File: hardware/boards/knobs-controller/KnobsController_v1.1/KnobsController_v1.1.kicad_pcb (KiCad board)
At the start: 2 copper layers, 110.5 x 54.3 mm, 71 parts, among them J1 ZX62-AB-5PA(31), J4 JST---S4B-PH-SM4-TB(LF)(SN)_J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, U2 MK1_ZERO_AP7215-33YG-13, U3 MK1_ZERO_ATSAMD21G18A-48, Y1 32.768KHz

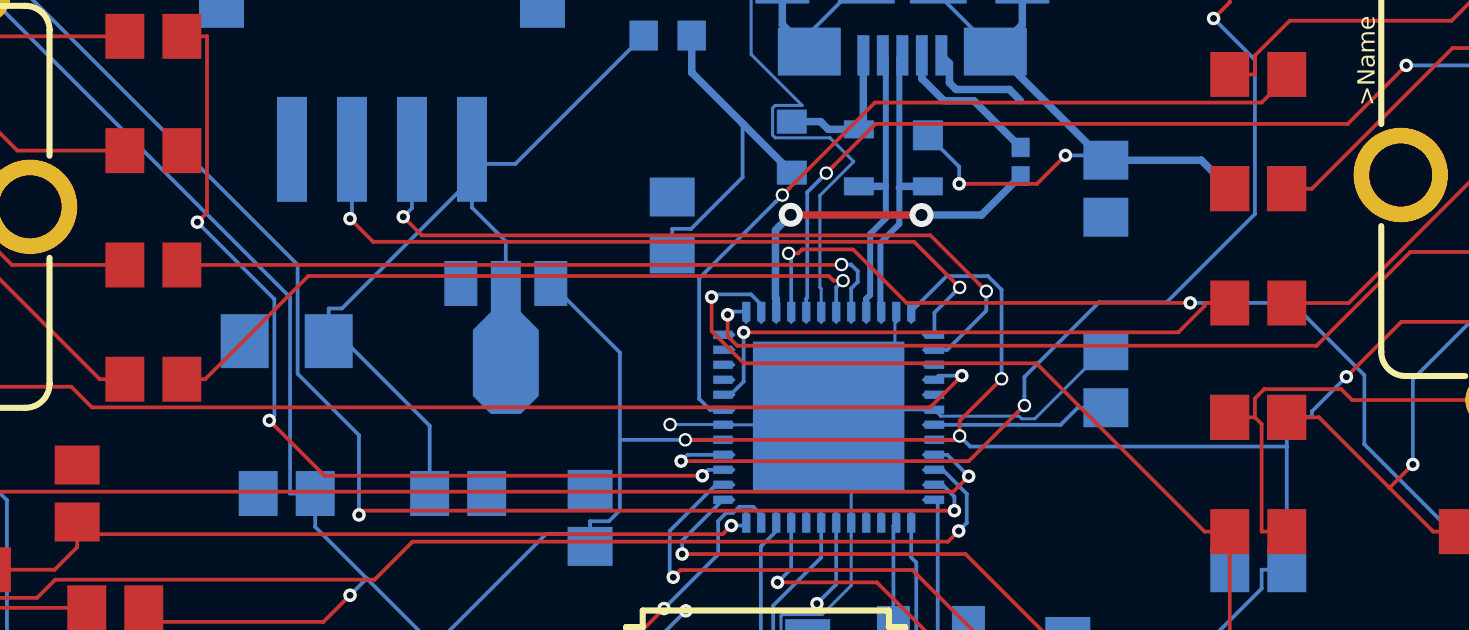
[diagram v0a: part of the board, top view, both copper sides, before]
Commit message: fixed unconnected traces
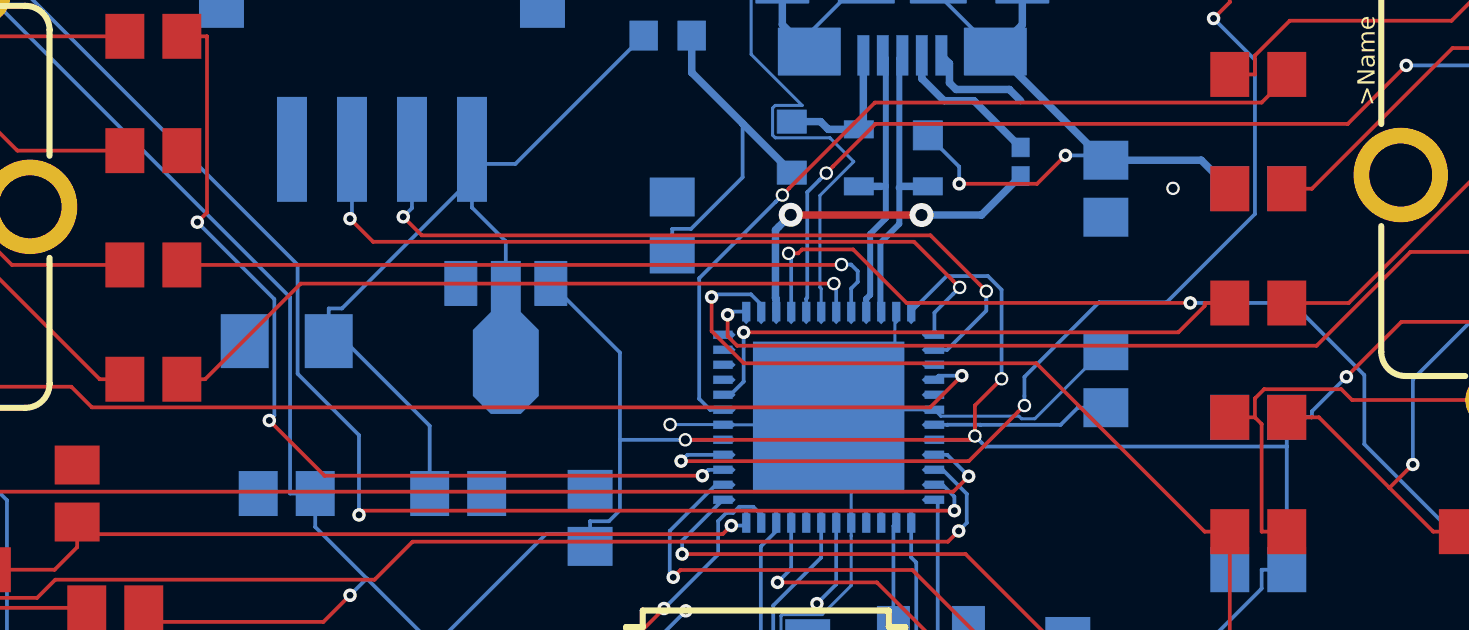
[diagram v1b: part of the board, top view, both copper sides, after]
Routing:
- net PA22_TC4-W0: track 24.7 -> 24.0 mm
- net GND: vias 1 -> 2
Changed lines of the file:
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@@
     (thickness 1.6)
     (drawings 240)
-    (tracks 659)
+    (tracks 663)
     (zones 0)
     (modules 71)
@@
     (31 Bottom signal)
     (32 B.Adhes user)
-    (33 F.Adhes user hide)
+    (33 F.Adhes user)
     (34 B.Paste user)
     (35 F.Paste user)
@@
   )
   (setup
-    (last_trace_width 0.1016)
+    (last_trace_width 0.0889)
     (user_trace_width 0.1016)
     (user_trace_width 0.2032)
@@
     (effects (font (size 1.6891 1.6891) (thickness 0.14224)) (justify left bottom))
   )
-  (via (at 154.432 112.776) (size 0.45) (drill 0.3) (layers Top Bottom) (net 25))
   (segment (start 153.821 100.087) (end 154.092 100.358) (width 0.25) (layer Bottom) (net 1))
   (segment (start 154.092 100.358) (end 154.092 101.006) (width 0.25) (layer Bottom) (net 1))
@@
   (segment (start 153.80171 112.11471) (end 156.405952 112.11471) (width 0.1016) (layer Bottom) (net 1))
   (segment (start 153.591 111.904) (end 153.80171 112.11471) (width 0.1016) (layer Bottom) (net 1))
+  (via (at 161.544 104.521) (size 0.45) (drill 0.3) (layers Top Bottom) (net 1))
   (segment (start 154.2562 115.2656) (end 154.2562 114.7965) (width 0.125) (layer Bottom) (net 4))
   (segment (start 154.2562 114.7965) (end 153.8637 114.404) (width 0.125) (layer Bottom) (net 4))
@@
   (segment (start 124.2638 117.234) (end 125.016 116.4818) (width 0.125) (layer Top) (net 9))
   (via (at 146.8211 115.7612) (size 0.45) (layers Top Bottom) (net 9))
-  (segment (start 129.281 110.884) (end 132.722946 107.442054) (width 0.125) (layer Top) (net 10))
-  (segment (start 150.070956 107.442054) (end 150.226506 107.597604) (width 0.125) (layer Top) (net 10))
+  (segment (start 150.316 108.629) (end 150.316 107.771) (width 0.125) (layer Bottom) (net 10))
+  (via (at 150.241 107.696) (size 0.45) (drill 0.3) (layers Top Bottom) (net 10))
   (segment (start 128.506 110.884) (end 129.281 110.884) (width 0.125) (layer Top) (net 10))
-  (segment (start 150.226506 107.597604) (end 150.544704 107.597604) (width 0.125) (layer Top) (net 10))
-  (segment (start 132.722946 107.442054) (end 150.070956 107.442054) (width 0.125) (layer Top) (net 10))
-  (segment (start 150.316 107.826308) (end 150.319705 107.822603) (width 0.125) (layer Bottom) (net 10))
-  (via (at 150.544704 107.597604) (size 0.45) (drill 0.3) (layers Top Bottom) (net 10))
-  (segment (start 150.319705 107.822603) (end 150.544704 107.597604) (width 0.125) (layer Bottom) (net 10))
-  (segment (start 150.316 108.629) (end 150.316 107.826308) (width 0.125) (layer Bottom) (net 10))
-  (via (at 150.495 107.061) (size 0.45) (drill 0.3) (layers Top Bottom) (net 11))
-  (segment (start 150.482 107.074) (end 150.495 107.061) (width 0.125) (layer Top) (net 11))
-  (segment (start 151.034531 107.282333) (end 150.813198 107.061) (width 0.125) (layer Bottom) (net 11))
-  (segment (start 128.506 107.074) (end 150.482 107.074) (width 0.125) (layer Top) (net 11))
-  (segment (start 150.816 107.858532) (end 151.034531 107.640001) (width 0.125) (layer Bottom) (net 11))
-  (segment (start 150.813198 107.061) (end 150.495 107.061) (width 0.125) (layer Bottom) (net 11))
+  (segment (start 150.316 107.771) (end 150.241 107.696) (width 0.125) (layer Bottom) (net 10))
+  (segment (start 129.281 110.884) (end 132.469 107.696) (width 0.125) (layer Top) (net 10))
+  (segment (start 132.469 107.696) (end 150.241 107.696) (width 0.125) (layer Top) (net 10))
+  (segment (start 150.813196 107.060976) (end 150.494998 107.060976) (width 0.125) (layer Bottom) (net 11))
+  (segment (start 151.034531 107.640001) (end 151.034531 107.282311) (width 0.125) (layer Bottom) (net 11))
+  (segment (start 150.481974 107.074) (end 150.494998 107.060976) (width 0.125) (layer Top) (net 11))
+  (segment (start 128.506 107.074) (end 150.481974 107.074) (width 0.125) (layer Top) (net 11))
   (segment (start 150.816 108.629) (end 150.816 107.858532) (width 0.125) (layer Bottom) (net 11))
-  (segment (start 151.034531 107.640001) (end 151.034531 107.282333) (width 0.125) (layer Bottom) (net 11))
+  (segment (start 151.034531 107.282311) (end 150.813196 107.060976) (width 0.125) (layer Bottom) (net 11))
+  (segment (start 150.816 107.858532) (end 151.034531 107.640001) (width 0.125) (layer Bottom) (net 11))
+  (via (at 150.494998 107.060976) (size 0.45) (drill 0.3) (layers Top Bottom) (net 11))
   (segment (start 128.506 99.4543) (end 129.3438 99.4543) (width 0.125) (layer Top) (net 12))
   (segment (start 145.8557 114.1008) (end 146.0525 113.904) (width 0.125) (layer Bottom) (net 12))
@@
   (via (at 167.3244 110.8038) (size 0.45) (layers Top Bottom) (net 25))
   (via (at 198.3232 112.0616) (size 0.45) (layers Top Bottom) (net 25))
-  (segment (start 154.304 112.904) (end 153.591 112.904) (width 0.125) (layer Bottom) (net 25))
-  (segment (start 154.432 112.776) (end 154.304 112.904) (width 0.125) (layer Bottom) (net 25))
-  (segment (start 154.7837 113.1277) (end 154.432 112.776) (width 0.125) (layer Bottom) (net 25))
-  (segment (start 165.336 113.1277) (end 154.7837 113.1277) (width 0.125) (layer Bottom) (net 25))
   (segment (start 155.829 110.871) (end 155.829 110.871) (width 0.125) (layer Top) (net 25))
   (via (at 155.829 110.871) (size 0.45) (drill 0.3) (layers Top Bottom) (net 25))
@@
   (segment (start 145.287 112.904) (end 143.1069 112.904) (width 0.125) (layer Bottom) (net 25))
   (via (at 145.287 112.904) (size 0.45) (drill 0.3) (layers Top Bottom) (net 25))
-  (segment (start 154.304 112.904) (end 154.432 112.776) (width 0.125) (layer Top) (net 25))
-  (segment (start 145.287 112.904) (end 154.304 112.904) (width 0.125) (layer Top) (net 25))
-  (segment (start 154.432 112.268) (end 155.829 110.871) (width 0.125) (layer Top) (net 25))
-  (segment (start 154.432 112.776) (end 154.432 112.268) (width 0.125) (layer Top) (net 25))
-  (segment (start 159.306 111.834) (end 158.3682 111.834) (width 0.125) (layer Bottom) (net 26))
+  (segment (start 154.812 112.904) (end 154.94 112.776) (width 0.125) (layer Top) (net 25))
+  (via (at 154.94 112.776) (size 0.45) (drill 0.3) (layers Top Bottom) (net 25))
+  (segment (start 165.336 113.1277) (end 155.2917 113.1277) (width 0.125) (layer Bottom) (net 25))
+  (segment (start 154.812 112.904) (end 154.94 112.776) (width 0.125) (layer Bottom) (net 25))
+  (segment (start 155.829 110.871) (end 154.94 111.76) (width 0.125) (layer Top) (net 25))
+  (segment (start 145.287 112.904) (end 154.812 112.904) (width 0.125) (layer Top) (net 25))
+  (segment (start 154.94 111.76) (end 154.94 112.457802) (width 0.125) (layer Top) (net 25))
+  (segment (start 154.94 112.457802) (end 154.94 112.776) (width 0.125) (layer Top) (net 25))
+  (segment (start 153.591 112.904) (end 154.812 112.904) (width 0.125) (layer Bottom) (net 25))
+  (segment (start 155.2917 113.1277) (end 155.164999 113.000999) (width 0.125) (layer Bottom) (net 25))
+  (segment (start 155.164999 113.000999) (end 154.94 112.776) (width 0.125) (layer Bottom) (net 25))
   (segment (start 158.3682 111.834) (end 157.7982 112.404) (width 0.125) (layer Bottom) (net 26))
-  (segment (start 157.7982 112.404) (end 153.591 112.404) (width 0.125) (layer Bottom) (net 26))
+  (segment (start 159.306 111.834) (end 158.3682 111.834) (width 0.125) (layer Bottom) (net 26))
+  (segment (start 154.020402 112.399598) (end 154.016 112.404) (width 0.125) (layer Bottom) (net 26))
+  (segment (start 155.125076 112.404) (end 155.120674 112.399598) (width 0.125) (layer Bottom) (net 26))
+  (segment (start 155.120674 112.399598) (end 154.020402 112.399598) (width 0.125) (layer Bottom) (net 26))
+  (segment (start 157.7982 112.404) (end 155.125076 112.404) (width 0.125) (layer Bottom) (net 26))
+  (segment (start 154.016 112.404) (end 153.591 112.404) (width 0.125) (layer Bottom) (net 26))
   (segment (start 138.8885 120.1465) (end 138.8885 122.5232) (width 0.125) (layer Bottom) (net 27))
   (segment (start 138.516 119.774) (end 138.8885 120.1465) (width 0.125) (layer Bottom) (net 27))

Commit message: added logo svg
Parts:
- added REF**: OpenSourceHardwareLogo, OpenSourceHardwareLogo:OpenSourceHardwareLogo, F.Cu at (151.0, 109.7)
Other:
- board text added: "v1.2"
- board text removed: "v1.1"
